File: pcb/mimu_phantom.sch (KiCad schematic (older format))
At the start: 0 parts

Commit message: I hope this did not break everything
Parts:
- added C_B1: 100nF, Capacitor_SMD:C_1206_3216Metric_Pad1.42x1.75mm_HandSolder, symbol Device:C
- added C_IN1, C_IN2, C_out1, C_out2: 10uF, Capacitor_SMD:C_1206_3216Metric_Pad1.42x1.75mm_HandSolder, symbol Device:C
- added D1: B1100, Diode_SMD:D_SMA, symbol Device:D_Schottky
- added D_B1: 1N4148, Diode_SMD:D_SMA, symbol Device:D
- added L1: 15uH, Inductor_SMD:L_7.3x7.3_H4.5, symbol Device:L
- added R_1: 10, Resistor_SMD:R_1206_3216Metric_Pad1.42x1.75mm_HandSolder, symbol Device:R
- added R_BOT1: 10k, Resistor_SMD:R_1206_3216Metric_Pad1.42x1.75mm_HandSolder, symbol Device:R
- added R_TOP1: 31.2k, Resistor_SMD:R_1206_3216Metric_Pad1.42x1.75mm_HandSolder, symbol Device:R
- added U3: MCP16331CH, Package_TO_SOT_SMD:SOT-23-6, symbol Regulator_Switching:MCP16331CH
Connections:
- new net: C_B1.1, D_B1.1 (K), U3.1 (BOOST)
- new net: R_BOT1.1, R_TOP1.2, U3.3 (VFB)
- new net: C_B1.2, D1.1 (K), L1.2, U3.6 (SW)
- new net: R_1.2, R_TOP1.1
- new net +BATT: C_IN1.1, C_IN2.1, U3.5 (VIN)
- new net GND: C_IN1.2, C_IN2.2, C_out1.2, C_out2.2, D1.2 (A), R_BOT1.2, U3.2 (GND)
- new net VCC: C_out1.1, C_out2.1, D_B1.2 (A), L1.1, R_1.1

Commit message: Quick layout test
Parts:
- removed R_1: 10, Resistor_SMD:R_1206_3216Metric_Pad1.42x1.75mm_HandSolder, symbol Device:R
- added R3, R4: 6.8Ohm 0.1%, Resistor_SMD:R_1206_3216Metric_Pad1.42x1.75mm_HandSolder, symbol Device:R
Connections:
- net +BATT: now also R3.2, R4.2
- net VCC: now also R_TOP1.1
- new net XLR_COLD: R4.1
- new net XLR_HOT: R3.1
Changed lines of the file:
@@
-$EndComp
-$Comp
-L Device:R R_1
-U 1 1 5E6AE12D
-P 4750 3100
-F 0 "R_1" H 4820 3146 50  0000 L CNN
-F 1 "10" H 4820 3055 50  0000 L CNN
-F 2 "Resistor_SMD:R_1206_3216Metric_Pad1.42x1.75mm_HandSolder" V 4680 3100 50  0001 C CNN
-F 3 "~" H 4750 3100 50  0001 C CNN
-	1    4750 3100
-	1    0    0    -1
 $EndComp
 $Comp
@@
 	1    0    0    -1
 $EndComp
-Connection ~ 4750 2950
-Wire Wire Line
-	4750 2950 4250 2950
-Wire Wire Line
-	4750 3350 4750 3250
 Wire Wire Line
 	2900 2950 3100 2950
@@
 	0    1    1    0
 $EndComp
+Text GLabel 1150 1250 1    50   Input ~ 0
+XLR_HOT
+Text GLabel 1400 1250 1    50   Input ~ 0
+XLR_COLD
+Text GLabel 1650 1250 1    50   Input ~ 0
+XLR_GND
+$Comp
+L power:+BATT #PWR0101
+U 1 1 5E6CDE97
+P 850 2700
+F 0 "#PWR0101" H 850 2550 50  0001 C CNN
+F 1 "+BATT" H 865 2873 50  0000 C CNN
+F 2 "" H 850 2700 50  0001 C CNN
+F 3 "" H 850 2700 50  0001 C CNN
+	1    850  2700
+	1    0    0    -1
+$EndComp
+$Comp
+L power:+BATT #PWR0102
+U 1 1 5E6CE2D2
+P 900 2000
+F 0 "#PWR0102" H 900 1850 50  0001 C CNN
+F 1 "+BATT" V 915 2127 50  0000 L CNN
+F 2 "" H 900 2000 50  0001 C CNN
+F 3 "" H 900 2000 50  0001 C CNN
+	1    900  2000
+	0    -1   -1   0
+$EndComp
+Wire Wire Line
+	850  2850 850  2700
+$Comp
+L Device:R R3
+U 1 1 5E6CFBA0
+P 1150 1550
+F 0 "R3" H 1000 1600 50  0000 L CNN
+F 1 "6.8Ohm 0.1%" H 600 1500 50  0000 L CNN
+F 2 "Resistor_SMD:R_1206_3216Metric_Pad1.42x1.75mm_HandSolder" V 1080 1550 50  0001 C CNN
+F 3 "e.g. KOA Speer RS73 High-Precision Flat Chip Resistors" H 1150 1550 50  0001 C CNN
+	1    1150 1550
+	1    0    0    -1
+$EndComp
+$Comp
+L Device:R R4
+U 1 1 5E6D0E42
+P 1400 1550
+F 0 "R4" H 1470 1596 50  0000 L CNN
+F 1 "6.8Ohm 0.1%" H 1470 1505 50  0000 L CNN
+F 2 "Resistor_SMD:R_1206_3216Metric_Pad1.42x1.75mm_HandSolder" V 1330 1550 50  0001 C CNN
+F 3 "e.g. KOA Speer RS73 High-Precision Flat Chip Resistors" H 1400 1550 50  0001 C CNN
+	1    1400 1550
+	1    0    0    -1
+$EndComp
+Wire Wire Line
+	1400 1400 1400 1250
+Wire Wire Line
+	1150 1250 1150 1400
+Wire Wire Line
+	1150 1700 1150 1850
+Wire Wire Line
+	1150 1850 1300 1850
+Wire Wire Line
+	1400 1850 1400 1700
+Wire Wire Line
+	1300 1850 1300 2000
+Wire Wire Line
+	1300 2000 900  2000
+Connection ~ 1300 1850
+Wire Wire Line
+	1300 1850 1400 1850
+$Comp
+L power:GND #PWR0107
+U 1 1 5E6DA84C
+P 1650 1850
+F 0 "#PWR0107" H 1650 1600 50  0001 C CNN
+F 1 "GND" H 1655 1677 50  0000 C CNN
+F 2 "" H 1650 1850 50  0001 C CNN
+F 3 "" H 1650 1850 50  0001 C CNN
+	1    1650 1850
+	1    0    0    -1
+$EndComp
+Wire Wire Line
+	1650 1850 1650 1250
+Wire Wire Line
+	4250 2950 4750 2950
+Wire Wire Line
+	4750 2950 4750 3350
+Connection ~ 4750 2950
 Wire Wire Line
 	4750 2950 4850 2950
-$Comp
-L power:+BATT #PWR01
-U 1 1 5E6A6C96
-P 850 2850
-F 0 "#PWR01" H 850 2700 50  0001 C CNN
-F 1 "+BATT" H 865 3023 50  0000 C CNN
-F 2 "" H 850 2850 50  0001 C CNN
-F 3 "" H 850 2850 50  0001 C CNN
-	1    850  2850
-	1    0    0    -1
-$EndComp
 $EndSCHEMATC

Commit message: Now it just has to work, lol
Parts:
- added TP1, TP3, TP4: TestPoint, Measurement_Points:Measurement_Point_Round-SMD-Pad_Small, symbol Connector:TestPoint
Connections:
- net +BATT: now also TP1.1
- net VCC: now also TP3.1
- net at R_BOT1.1, R_TOP1.2, U3.3 (VFB): now also TP4.1
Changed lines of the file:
@@
 $EndDescr
 $Sheet
-S 6500 2100 3800 1600
+S 6100 2000 3800 1600
 U 5E6CC751
 F0 "Mimu_base" 50
@@
 Wire Wire Line
 	1100 3150 1100 3300
-Wire Wire Line
-	1550 2850 2100 2850
 Connection ~ 1550 2850
 $Comp
@@
 Wire Wire Line
 	4750 2950 4850 2950
+$Comp
+L Connector:TestPoint TP1
+U 1 1 5E6D2D69
+P 1300 2000
+F 0 "TP1" H 1242 2026 50  0000 R CNN
+F 1 "TestPoint" H 1242 2117 50  0000 R CNN
+F 2 "Measurement_Points:Measurement_Point_Round-SMD-Pad_Small" H 1500 2000 50  0001 C CNN
+F 3 "~" H 1500 2000 50  0001 C CNN
+	1    1300 2000
+	-1   0    0    1
+$EndComp
+Connection ~ 1300 2000
+$Comp
+L Connector:TestPoint TP4
+U 1 1 5E6D362C
+P 2950 3700
+F 0 "TP4" V 2750 3850 50  0000 C CNN
+F 1 "TestPoint" V 2850 3750 50  0000 C CNN
+F 2 "Measurement_Points:Measurement_Point_Round-SMD-Pad_Small" H 3150 3700 50  0001 C CNN
+F 3 "~" H 3150 3700 50  0001 C CNN
+	1    2950 3700
+	0    -1   -1   0
+$EndComp
+Connection ~ 2950 3700
+$Comp
+L Connector:TestPoint TP3
+U 1 1 5E6D91F6
+P 4750 2950
+F 0 "TP3" H 4700 3150 50  0000 L CNN
+F 1 "TestPoint" H 4700 3250 50  0000 L CNN
+F 2 "Measurement_Points:Measurement_Point_Round-SMD-Pad_Small" H 4950 2950 50  0001 C CNN
+F 3 "~" H 4950 2950 50  0001 C CNN
+	1    4750 2950
+	1    0    0    -1
+$EndComp
+Wire Wire Line
+	1550 2850 2100 2850
 $EndSCHEMATC

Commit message: Buy all the shit
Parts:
- added C4, C5, C6: 0.1uF, Capacitors_THT:CP_Radial_D4.0mm_P2.00mm, symbol Device:CP
- D1: footprint Diode_SMD:D_SMA -> Diodes_SMD:D_SMA
- D_B1: footprint Diode_SMD:D_SMA -> Diodes_SMD:D_SOD-323_HandSoldering
- L1: footprint Inductor_SMD:L_7.3x7.3_H4.5 -> Inductors_SMD:L_7.3x7.3_H4.5
- R3, R4: footprint Resistor_SMD:R_1206_3216Metric_Pad1.42x1.75mm_HandSolder -> Resistors_THT:R_Axial_DIN0207_L6.3mm_D2.5mm_P7.62mm_Horizontal
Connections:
- net +BATT: now also C4.1, C5.1, C6.1
- net GND: now also C4.2, C5.2, C6.2
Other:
- moved on the sheet: R3, R4, TP1
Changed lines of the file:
@@
 F 0 "D_B1" H 3750 2766 50  0000 C CNN
 F 1 "1N4148" H 3750 2675 50  0000 C CNN
-F 2 "Diode_SMD:D_SMA" H 3750 2550 50  0001 C CNN
+F 2 "Diodes_SMD:D_SOD-323_HandSoldering" H 3750 2550 50  0001 C CNN
 F 3 "~" H 3750 2550 50  0001 C CNN
 	1    3750 2550
@@
 F 0 "L1" V 3450 2950 50  0000 C CNN
 F 1 "15uH" V 3260 2950 50  0000 C CNN
-F 2 "Inductor_SMD:L_7.3x7.3_H4.5" H 3350 2950 50  0001 C CNN
+F 2 "Inductors_SMD:L_7.3x7.3_H4.5" H 3350 2950 50  0001 C CNN
 F 3 "Würth 7447779115" H 3350 2950 50  0001 C CNN
 	1    3350 2950
@@
 F 0 "D1" V 3054 3279 50  0000 L CNN
 F 1 "B1100" V 3145 3279 50  0000 L CNN
-F 2 "Diode_SMD:D_SMA" H 3100 3200 50  0001 C CNN
+F 2 "Diodes_SMD:D_SMA" H 3100 3200 50  0001 C CNN
 F 3 "~" H 3100 3200 50  0001 C CNN
 	1    3100 3200
@@
 	0    1    1    0
 $EndComp
-Text GLabel 1150 1250 1    50   Input ~ 0
+Text GLabel 2150 1050 1    50   Input ~ 0
 XLR_HOT
-Text GLabel 1400 1250 1    50   Input ~ 0
+Text GLabel 2400 1050 1    50   Input ~ 0
 XLR_COLD
-Text GLabel 1650 1250 1    50   Input ~ 0
+Text GLabel 2650 1050 1    50   Input ~ 0
 XLR_GND
 $Comp
 L power:+BATT #PWR0101
 U 1 1 5E6CDE97
-P 850 2700
-F 0 "#PWR0101" H 850 2550 50  0001 C CNN
-F 1 "+BATT" H 865 2873 50  0000 C CNN
-F 2 "" H 850 2700 50  0001 C CNN
-F 3 "" H 850 2700 50  0001 C CNN
-	1    850  2700
+P 850 2800
+F 0 "#PWR0101" H 850 2650 50  0001 C CNN
+F 1 "+BATT" H 865 2973 50  0000 C CNN
+F 2 "" H 850 2800 50  0001 C CNN
+F 3 "" H 850 2800 50  0001 C CNN
+	1    850  2800
 	1    0    0    -1
 $EndComp
@@
 L power:+BATT #PWR0102
 U 1 1 5E6CE2D2
-P 900 2000
-F 0 "#PWR0102" H 900 1850 50  0001 C CNN
-F 1 "+BATT" V 915 2127 50  0000 L CNN
-F 2 "" H 900 2000 50  0001 C CNN
-F 3 "" H 900 2000 50  0001 C CNN
-	1    900  2000
+P 1200 1800
+F 0 "#PWR0102" H 1200 1650 50  0001 C CNN
+F 1 "+BATT" V 1215 1927 50  0000 L CNN
+F 2 "" H 1200 1800 50  0001 C CNN
+F 3 "" H 1200 1800 50  0001 C CNN
+	1    1200 1800
 	0    -1   -1   0
 $EndComp
 Wire Wire Line
-	850  2850 850  2700
+	850  2850 850  2800
 $Comp
 L Device:R R3
 U 1 1 5E6CFBA0
-P 1150 1550
-F 0 "R3" H 1000 1600 50  0000 L CNN
-F 1 "6.8Ohm 0.1%" H 600 1500 50  0000 L CNN
-F 2 "Resistor_SMD:R_1206_3216Metric_Pad1.42x1.75mm_HandSolder" V 1080 1550 50  0001 C CNN
-F 3 "e.g. KOA Speer RS73 High-Precision Flat Chip Resistors" H 1150 1550 50  0001 C CNN
-	1    1150 1550
+P 2150 1350
+F 0 "R3" H 2000 1400 50  0000 L CNN
+F 1 "6.8Ohm 0.1%" H 1600 1300 50  0000 L CNN
+F 2 "Resistors_THT:R_Axial_DIN0207_L6.3mm_D2.5mm_P7.62mm_Horizontal" V 2080 1350 50  0001 C CNN
+F 3 "e.g. KOA Speer RS73 High-Precision Flat Chip Resistors" H 2150 1350 50  0001 C CNN
+	1    2150 1350
 	1    0    0    -1
 $EndComp
@@
 L Device:R R4
 U 1 1 5E6D0E42
-P 1400 1550
-F 0 "R4" H 1470 1596 50  0000 L CNN
-F 1 "6.8Ohm 0.1%" H 1470 1505 50  0000 L CNN
-F 2 "Resistor_SMD:R_1206_3216Metric_Pad1.42x1.75mm_HandSolder" V 1330 1550 50  0001 C CNN
-F 3 "e.g. KOA Speer RS73 High-Precision Flat Chip Resistors" H 1400 1550 50  0001 C CNN
-	1    1400 1550
-	1    0    0    -1
-$EndComp
-Wire Wire Line
-	1400 1400 1400 1250
-Wire Wire Line
-	1150 1250 1150 1400
-Wire Wire Line
-	1150 1700 1150 1850
-Wire Wire Line
-	1150 1850 1300 1850
-Wire Wire Line
-	1400 1850 1400 1700
-Wire Wire Line
-	1300 1850 1300 2000
-Wire Wire Line
-	1300 2000 900  2000
-Connection ~ 1300 1850
-Wire Wire Line
-	1300 1850 1400 1850
+P 2400 1350
+F 0 "R4" H 2470 1396 50  0000 L CNN
+F 1 "6.8Ohm 0.1%" H 2470 1305 50  0000 L CNN
+F 2 "Resistors_THT:R_Axial_DIN0207_L6.3mm_D2.5mm_P7.62mm_Horizontal" V 2330 1350 50  0001 C CNN
+F 3 "e.g. KOA Speer RS73 High-Precision Flat Chip Resistors" H 2400 1350 50  0001 C CNN
+	1    2400 1350
+	1    0    0    -1
+$EndComp
+Wire Wire Line
+	2400 1200 2400 1050
+Wire Wire Line
+	2150 1050 2150 1200
+Wire Wire Line
+	2150 1500 2150 1650
+Wire Wire Line
+	2150 1650 2300 1650
+Wire Wire Line
+	2400 1650 2400 1500
+Wire Wire Line
+	2300 1650 2300 1800
+Connection ~ 2300 1650
+Wire Wire Line
+	2300 1650 2400 1650
 $Comp
 L power:GND #PWR0107
 U 1 1 5E6DA84C
-P 1650 1850
-F 0 "#PWR0107" H 1650 1600 50  0001 C CNN
-F 1 "GND" H 1655 1677 50  0000 C CNN
-F 2 "" H 1650 1850 50  0001 C CNN
-F 3 "" H 1650 1850 50  0001 C CNN
-	1    1650 1850
-	1    0    0    -1
-$EndComp
-Wire Wire Line
-	1650 1850 1650 1250
+P 2650 1650
+F 0 "#PWR0107" H 2650 1400 50  0001 C CNN
+F 1 "GND" H 2655 1477 50  0000 C CNN
+F 2 "" H 2650 1650 50  0001 C CNN
+F 3 "" H 2650 1650 50  0001 C CNN
+	1    2650 1650
+	1    0    0    -1
+$EndComp
+Wire Wire Line
+	2650 1650 2650 1050
 Wire Wire Line
 	4250 2950 4750 2950
@@
 L Connector:TestPoint TP1
 U 1 1 5E6D2D69
-P 1300 2000
-F 0 "TP1" H 1242 2026 50  0000 R CNN
-F 1 "TestPoint" H 1242 2117 50  0000 R CNN
-F 2 "Measurement_Points:Measurement_Point_Round-SMD-Pad_Small" H 1500 2000 50  0001 C CNN
-F 3 "~" H 1500 2000 50  0001 C CNN
-	1    1300 2000
+P 2300 1800
+F 0 "TP1" H 2242 1826 50  0000 R CNN
+F 1 "TestPoint" H 2242 1917 50  0000 R CNN
+F 2 "Measurement_Points:Measurement_Point_Round-SMD-Pad_Small" H 2500 1800 50  0001 C CNN
+F 3 "~" H 2500 1800 50  0001 C CNN
+	1    2300 1800
 	-1   0    0    1
 $EndComp
-Connection ~ 1300 2000
 $Comp
 L Connector:TestPoint TP4
@@
 Wire Wire Line
 	1550 2850 2100 2850
+$Comp
+L Device:CP C5
+U 1 1 5E71F447
+P 1300 1950
+F 0 "C5" H 1418 1996 50  0000 L CNN
+F 1 "0.1uF" H 1418 1905 50  0000 L CNN
+F 2 "Capacitors_THT:CP_Radial_D4.0mm_P2.00mm" H 1338 1800 50  0001 C CNN
+F 3 "~" H 1300 1950 50  0001 C CNN
+	1    1300 1950
+	1    0    0    -1
+$EndComp
+Connection ~ 1300 1800
+Wire Wire Line
+	1300 1800 1200 1800
+$Comp
+L power:GND #PWR0108
+U 1 1 5E71FAE9
+P 1700 2200
+F 0 "#PWR0108" H 1700 1950 50  0001 C CNN
+F 1 "GND" H 1705 2027 50  0000 C CNN
+F 2 "" H 1700 2200 50  0001 C CNN
+F 3 "" H 1700 2200 50  0001 C CNN
+	1    1700 2200
+	1    0    0    -1
+$EndComp
+Wire Wire Line
+	1300 1800 1700 1800
+Connection ~ 2300 1800
+$Comp
+L Device:CP C4
+U 1 1 5E740344
+P 1700 1950
+F 0 "C4" H 1818 1996 50  0000 L CNN
+F 1 "0.1uF" H 1818 1905 50  0000 L CNN
+F 2 "Capacitors_THT:CP_Radial_D4.0mm_P2.00mm" H 1738 1800 50  0001 C CNN
+F 3 "~" H 1700 1950 50  0001 C CNN
+	1    1700 1950
+	1    0    0    -1
+$EndComp
+Connection ~ 1700 1800
+Wire Wire Line
+	1700 1800 2100 1800
+$Comp
+L Device:CP C6
+U 1 1 5E7407AD
+P 2100 1950
+F 0 "C6" H 2218 1996 50  0000 L CNN
+F 1 "0.1uF" H 2218 1905 50  0000 L CNN
+F 2 "Capacitors_THT:CP_Radial_D4.0mm_P2.00mm" H 2138 1800 50  0001 C CNN
+F 3 "~" H 2100 1950 50  0001 C CNN
+	1    2100 1950
+	1    0    0    -1
+$EndComp
+Connection ~ 2100 1800
+Wire Wire Line
+	2100 1800 2300 1800
+Wire Wire Line
+	2100 2100 1700 2100
+Wire Wire Line
+	1700 2100 1300 2100
+Connection ~ 1700 2100
+Wire Wire Line
+	1700 2200 1700 2100
 $EndSCHEMATC

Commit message: Something new about the PCB?
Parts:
- R3, R4: value 6.8Ohm 0.1% -> 6.8kOhm 0.1%
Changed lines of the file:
@@
 P 2150 1350
 F 0 "R3" H 2000 1400 50  0000 L CNN
-F 1 "6.8Ohm 0.1%" H 1600 1300 50  0000 L CNN
+F 1 "6.8kOhm 0.1%" H 1600 1300 50  0000 L CNN
 F 2 "Resistors_THT:R_Axial_DIN0207_L6.3mm_D2.5mm_P7.62mm_Horizontal" V 2080 1350 50  0001 C CNN
 F 3 "e.g. KOA Speer RS73 High-Precision Flat Chip Resistors" H 2150 1350 50  0001 C CNN
@@
 P 2400 1350
 F 0 "R4" H 2470 1396 50  0000 L CNN
-F 1 "6.8Ohm 0.1%" H 2470 1305 50  0000 L CNN
+F 1 "6.8kOhm 0.1%" H 2470 1305 50  0000 L CNN
 F 2 "Resistors_THT:R_Axial_DIN0207_L6.3mm_D2.5mm_P7.62mm_Horizontal" V 2330 1350 50  0001 C CNN
 F 3 "e.g. KOA Speer RS73 High-Precision Flat Chip Resistors" H 2400 1350 50  0001 C CNN

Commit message: This might actually work
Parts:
- removed C4, C5, C6: 0.1uF, Capacitors_THT:CP_Radial_D4.0mm_P2.00mm, symbol Device:CP
- added C_pre1: 100uF, Capacitor_SMD:C_1206_3216Metric_Pad1.33x1.80mm_HandSolder, symbol Device:C
- R3, R4: footprint Resistors_THT:R_Axial_DIN0207_L6.3mm_D2.5mm_P7.62mm_Horizontal -> Resistor_SMD:R_0805_2012Metric_Pad1.20x1.40mm_HandSolder
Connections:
- net +BATT: now also C_pre1.1
- net GND: now also C_pre1.2
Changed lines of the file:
@@
 F 0 "R3" H 2000 1400 50  0000 L CNN
 F 1 "6.8kOhm 0.1%" H 1600 1300 50  0000 L CNN
-F 2 "Resistors_THT:R_Axial_DIN0207_L6.3mm_D2.5mm_P7.62mm_Horizontal" V 2080 1350 50  0001 C CNN
-F 3 "e.g. KOA Speer RS73 High-Precision Flat Chip Resistors" H 2150 1350 50  0001 C CNN
+F 2 "Resistor_SMD:R_0805_2012Metric_Pad1.20x1.40mm_HandSolder" V 2080 1350 50  0001 C CNN
+F 3 "https://www.digikey.de/product-detail/en/susumu/RG2012P-682-B-T5/RG20P6-8KBDKR-ND/1241578" H 2150 1350 50  0001 C CNN
 	1    2150 1350
 	1    0    0    -1
@@
 F 0 "R4" H 2470 1396 50  0000 L CNN
 F 1 "6.8kOhm 0.1%" H 2470 1305 50  0000 L CNN
-F 2 "Resistors_THT:R_Axial_DIN0207_L6.3mm_D2.5mm_P7.62mm_Horizontal" V 2330 1350 50  0001 C CNN
+F 2 "Resistor_SMD:R_0805_2012Metric_Pad1.20x1.40mm_HandSolder" V 2330 1350 50  0001 C CNN
 F 3 "e.g. KOA Speer RS73 High-Precision Flat Chip Resistors" H 2400 1350 50  0001 C CNN
 	1    2400 1350
@@
 Wire Wire Line
 	1550 2850 2100 2850
+Connection ~ 2300 1800
 $Comp
-L Device:CP C5
-U 1 1 5E71F447
-P 1300 1950
-F 0 "C5" H 1418 1996 50  0000 L CNN
-F 1 "0.1uF" H 1418 1905 50  0000 L CNN
-F 2 "Capacitors_THT:CP_Radial_D4.0mm_P2.00mm" H 1338 1800 50  0001 C CNN
-F 3 "~" H 1300 1950 50  0001 C CNN
-	1    1300 1950
+L Device:C C_pre1
+U 1 1 61774024
+P 1700 1950
+F 0 "C_pre1" H 1815 1996 50  0000 L CNN
+F 1 "100uF" H 1815 1905 50  0000 L CNN
+F 2 "Capacitor_SMD:C_1206_3216Metric_Pad1.33x1.80mm_HandSolder" H 1738 1800 50  0001 C CNN
+F 3 "~" H 1700 1950 50  0001 C CNN
+	1    1700 1950
 	1    0    0    -1
 $EndComp
-Connection ~ 1300 1800
-Wire Wire Line
-	1300 1800 1200 1800
 $Comp
-L power:GND #PWR0108
-U 1 1 5E71FAE9
+L power:GND #PWR0103
+U 1 1 61774455
 P 1700 2200
-F 0 "#PWR0108" H 1700 1950 50  0001 C CNN
+F 0 "#PWR0103" H 1700 1950 50  0001 C CNN
 F 1 "GND" H 1705 2027 50  0000 C CNN
 F 2 "" H 1700 2200 50  0001 C CNN
@@
 $EndComp
 Wire Wire Line
-	1300 1800 1700 1800
-Connection ~ 2300 1800
-$Comp
-L Device:CP C4
-U 1 1 5E740344
-P 1700 1950
-F 0 "C4" H 1818 1996 50  0000 L CNN
-F 1 "0.1uF" H 1818 1905 50  0000 L CNN
-F 2 "Capacitors_THT:CP_Radial_D4.0mm_P2.00mm" H 1738 1800 50  0001 C CNN
-F 3 "~" H 1700 1950 50  0001 C CNN
-	1    1700 1950
-	1    0    0    -1
-$EndComp
+	1700 2100 1700 2200
 Connection ~ 1700 1800
 Wire Wire Line
-	1700 1800 2100 1800
-$Comp
-L Device:CP C6
-U 1 1 5E7407AD
-P 2100 1950
-F 0 "C6" H 2218 1996 50  0000 L CNN
-F 1 "0.1uF" H 2218 1905 50  0000 L CNN
-F 2 "Capacitors_THT:CP_Radial_D4.0mm_P2.00mm" H 2138 1800 50  0001 C CNN
-F 3 "~" H 2100 1950 50  0001 C CNN
-	1    2100 1950
-	1    0    0    -1
-$EndComp
-Connection ~ 2100 1800
+	1700 1800 2300 1800
 Wire Wire Line
-	2100 1800 2300 1800
-Wire Wire Line
-	2100 2100 1700 2100
-Wire Wire Line
-	1700 2100 1300 2100
-Connection ~ 1700 2100
-Wire Wire Line
-	1700 2200 1700 2100
+	1200 1800 1700 1800
 $EndSCHEMATC

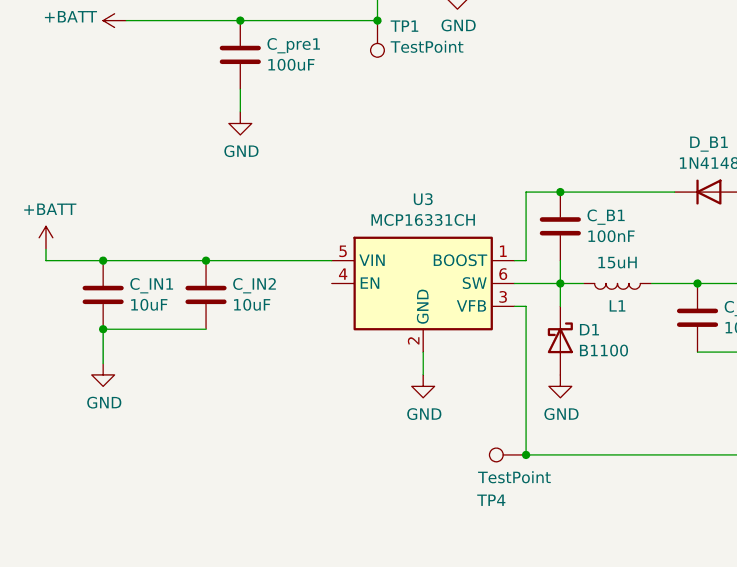
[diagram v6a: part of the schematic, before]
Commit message: Connected Attenuation to PWM-Able pin
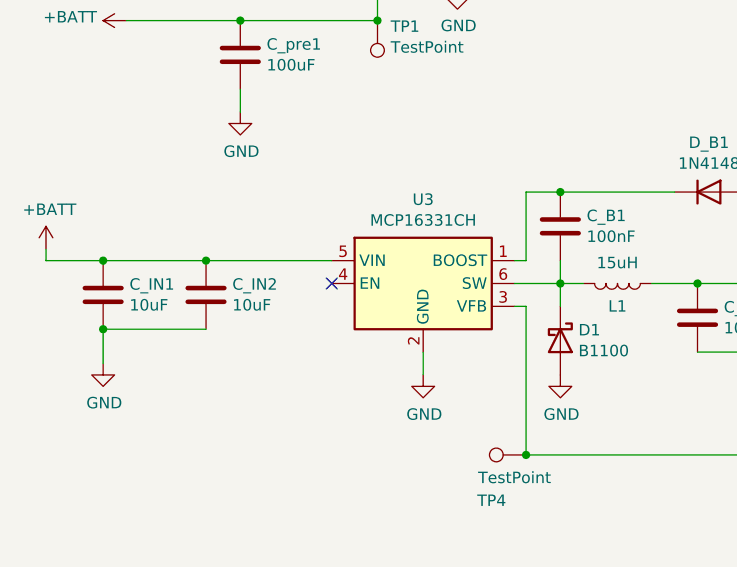
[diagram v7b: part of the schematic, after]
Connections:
- no-connect marks 0 -> 1
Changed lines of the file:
@@
 Wire Wire Line
 	1200 1800 1700 1800
+NoConn ~ 2100 2950
 $EndSCHEMATC

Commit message: First impression of new v3!
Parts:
- added C_pre2: 50-100uF @24V, Capacitor_SMD:C_1206_3216Metric_Pad1.33x1.80mm_HandSolder, symbol Device:C
- C_pre1: value 100uF -> 50-100uF @24V
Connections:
- net GND: now also C_pre2.2; no longer C_pre1.2
- new net: C_pre1.2, C_pre2.1
